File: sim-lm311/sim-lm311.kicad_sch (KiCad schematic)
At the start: 8 parts, among them U1 LM311

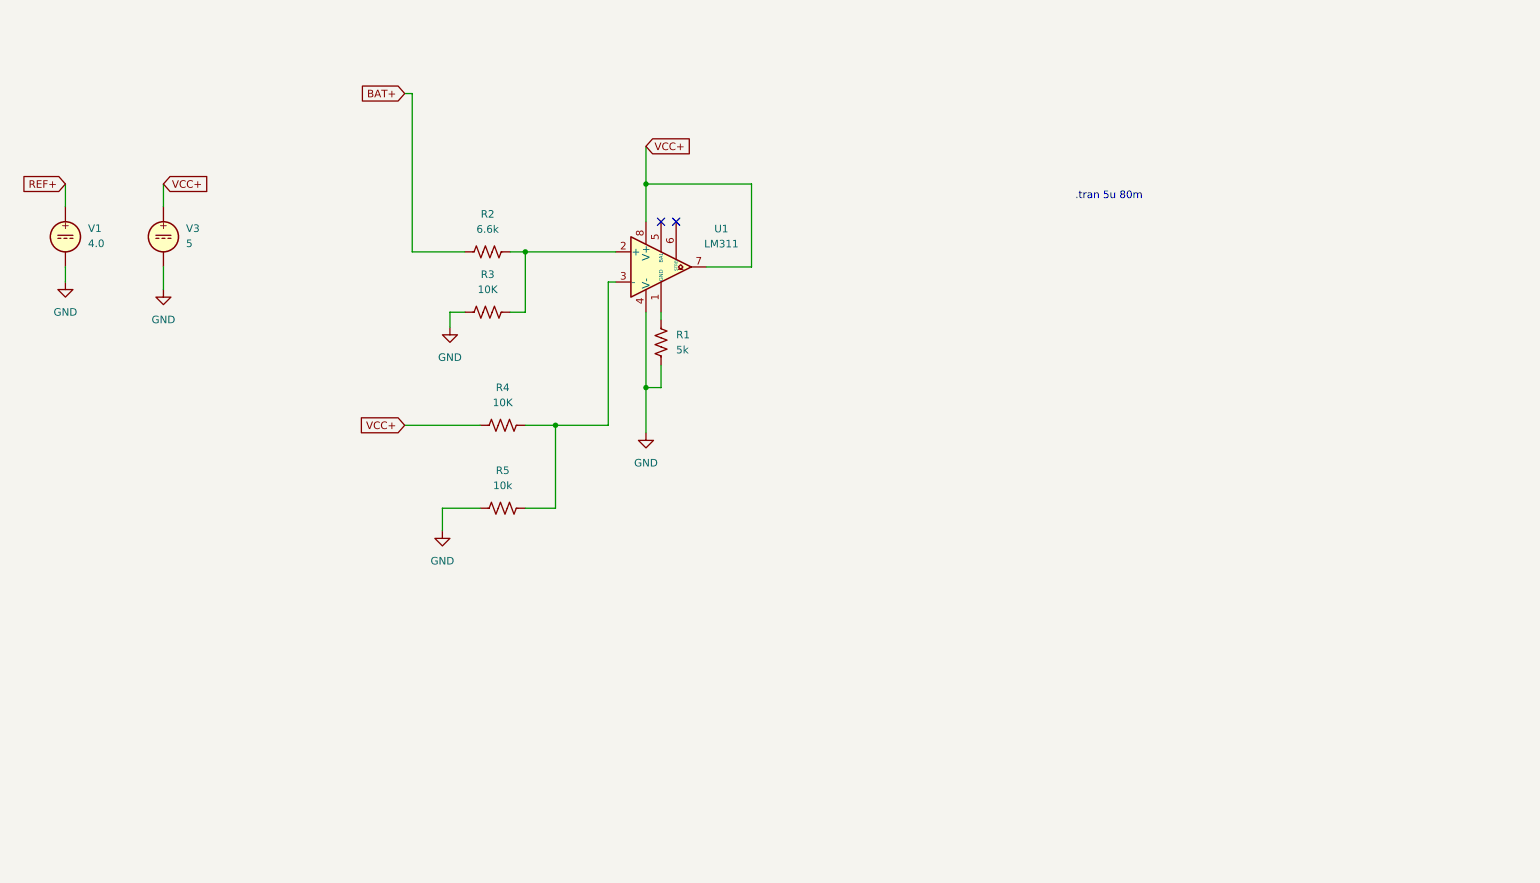
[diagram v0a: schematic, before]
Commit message: check folder lm311 for comparator schematics
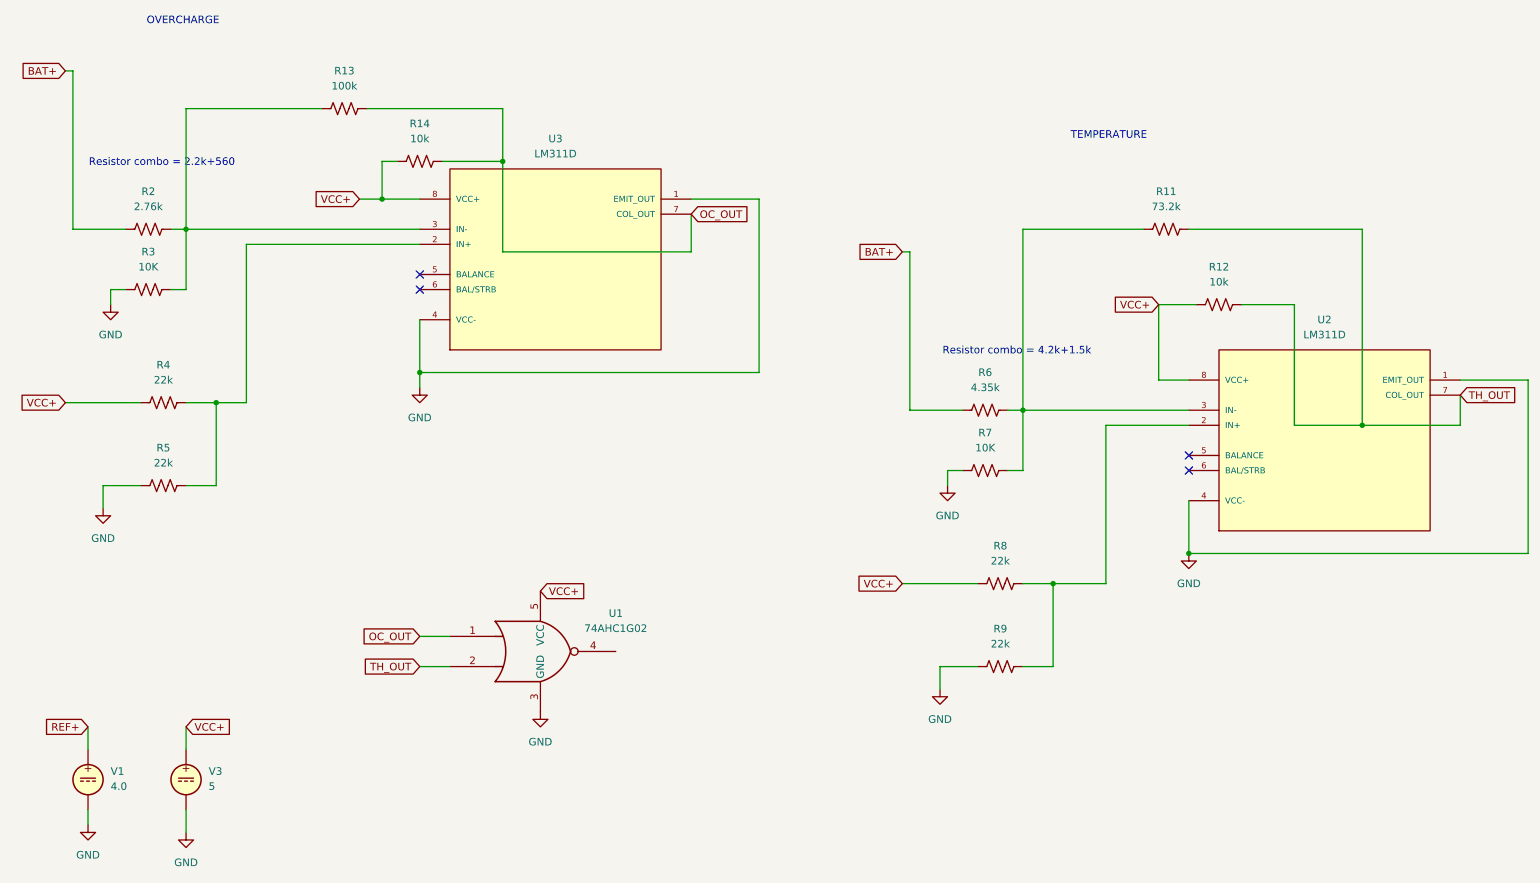
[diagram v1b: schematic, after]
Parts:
- removed R1: 5k, symbol Device:R_US
- removed U1: LM311, symbol Comparator:LM311
- added R11: 73.2k, symbol Device:R_US
- added R12, R14: 10k, symbol Device:R_US
- added R13: 100k, symbol Device:R_US
- added R6: 4.35k, symbol Device:R_US
- added R7: 10K, symbol Device:R_US
- added R8, R9: 22k, symbol Device:R_US
- added U1: 74AHC1G02, symbol 74xGxx:74AHC1G02
- added U2, U3: LM311D, LM311D:SOIC127P600X175-8N, symbol LM311D:LM311D
- R2: value 6.6k -> 2.76k
- R4: value 10K -> 22k
- R5: value 10k -> 22k
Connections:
- net BAT+: now also R6.1
- net GND: now also R7.1, R9.1, U1.3 (GND), U2.1 (EMIT_OUT), U2.4 (VCC-), U3.1 (EMIT_OUT), U3.4 (VCC-)
- net VCC+: now also R12.1, R14.1, R8.1, U1.5 (VCC), U2.8 (VCC+), U3.8 (VCC+)
- net at R2.2, R3.2: now also R13.1, U3.3 (IN-)
- net at R4.2, R5.2: now also U3.2 (IN+)
- new net: R8.2, R9.2, U2.2 (IN+)
- new net: R11.1, R6.2, R7.2, U2.3 (IN-)
- new net OC_OUT: R13.2, R14.2, U1.1, U3.7 (COL_OUT)
- new net TH_OUT: R11.2, R12.2, U1.2, U2.7 (COL_OUT)
- no-connect marks 2 -> 4
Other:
- note added: "OVERCHARGE"
- note added: "Resistor combo = 2.2k+560"
- note added: "Resistor combo = 4.2k+1.5k"
- note added: "TEMPERATURE"
- note removed: ".tran 5u 80m"
- moved on the sheet: R2, R3, R4, R5, V1, V3
